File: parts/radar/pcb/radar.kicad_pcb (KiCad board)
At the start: 2 copper layers, 65.5 x 25.5 mm, 10 parts, among them J1 RJ45_Shielded, J2 Conn_01x05

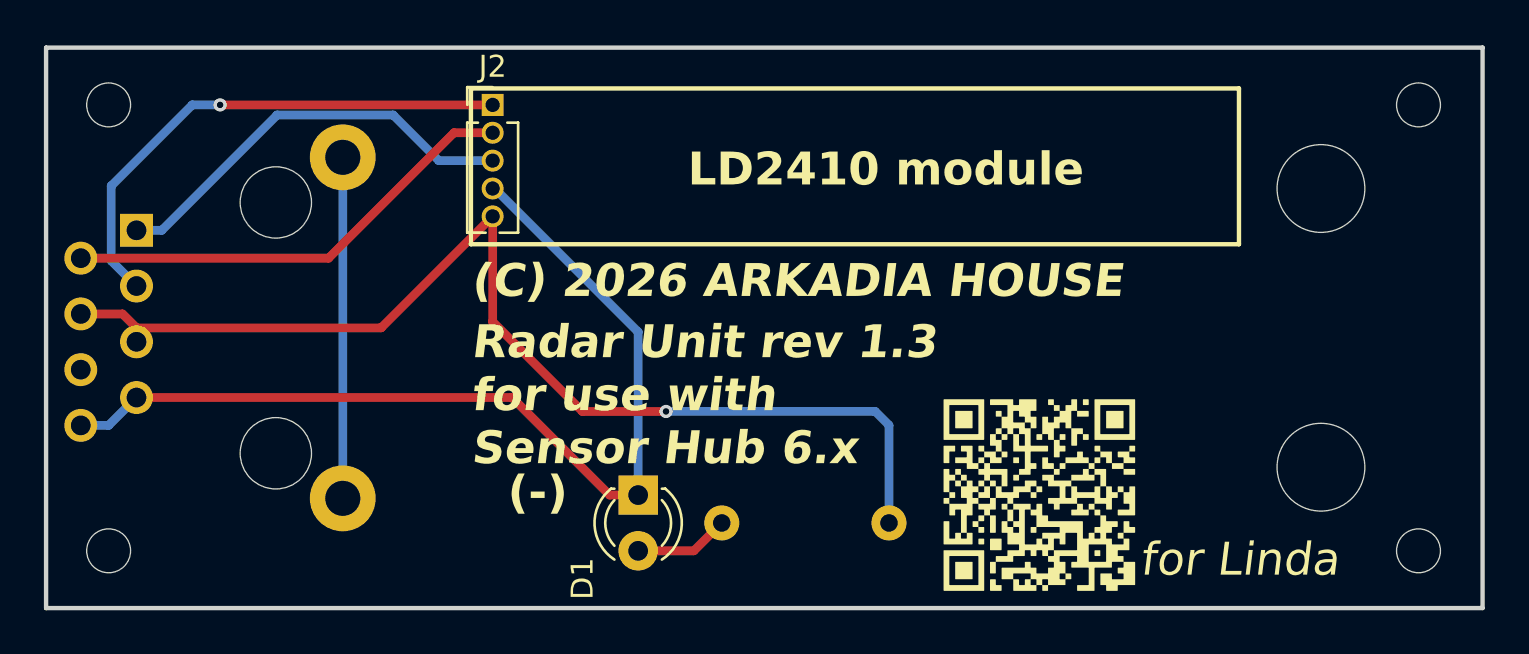
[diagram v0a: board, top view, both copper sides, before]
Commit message: pcb revisions to update to better RJ45 jack, update QR code.
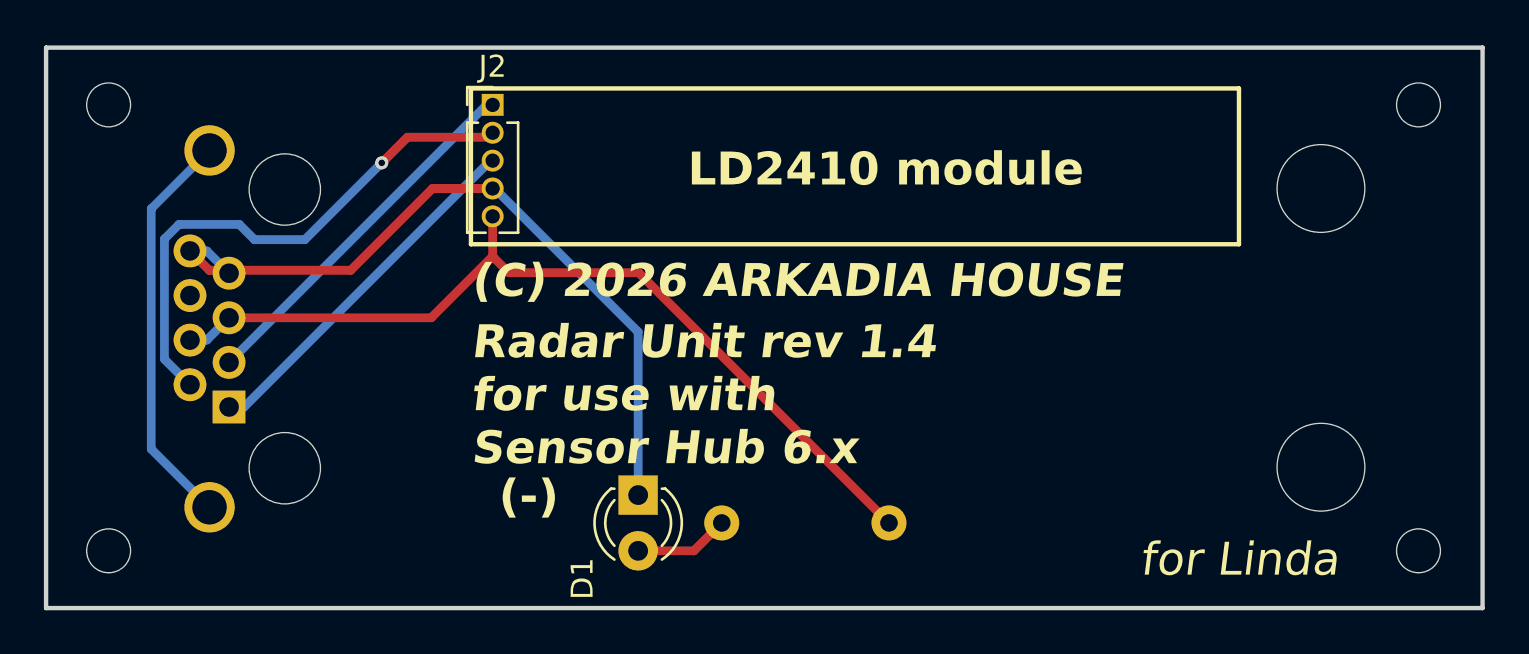
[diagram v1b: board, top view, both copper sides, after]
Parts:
- J1: footprint Connector_RJ:RJ45_Ninigi_GE -> Connector_RJ:RJ45_Amphenol_RJHSE5380
- moved J1 9.09 mm to (102.0, 53.1), turned to 90 degrees
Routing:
- net /VCC 5V: track 51.0 -> 40.3 mm, vias 1 -> 0
- net /GND: track 44.5 -> 34.6 mm
- net /OUT: track 24.0 -> 16.9 mm, vias 1 -> 0
- net /UART_TX: track 21.1 -> 24.4 mm, vias 0 -> 1
- net unconnected-(J1-PadSH): track 15.5 -> 18.5 mm
- net /UART_RX: track 19.3 -> 16.6 mm
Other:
- board text added: "Radar Unit rev 1.4 for use with Sensor Hub 6.x"
- board text removed: "Radar Unit rev 1.3 for use with Sensor Hub 6.x"
